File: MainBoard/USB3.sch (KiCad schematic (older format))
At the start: 16 parts, among them J10 USB3_A, J11 USB3_A (FAST), J5 USB3_A, J6 USB3_A, J8 USB3_A(INTEARNAL), J9 USB3_A, U4 TUSB8041, U5 UPD720201K8-711-BAC-A, U6 MX25L5121EMC-20G, Y1 24Mhz

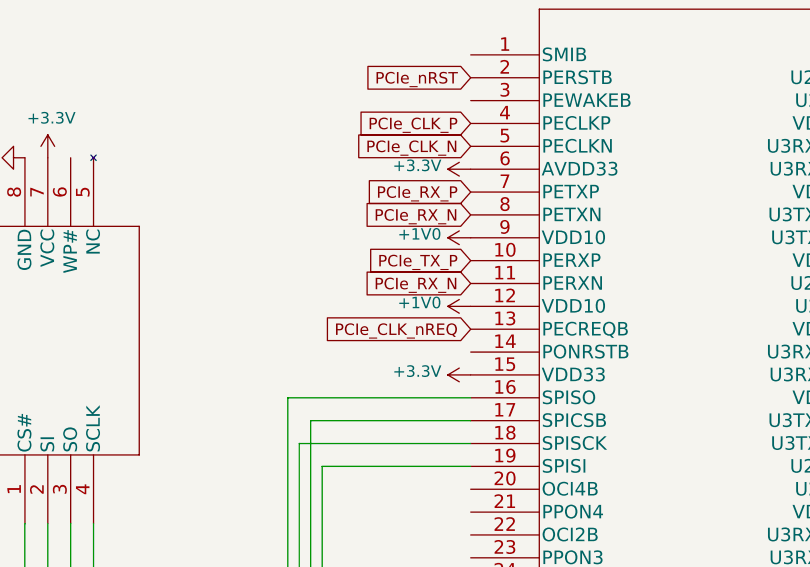
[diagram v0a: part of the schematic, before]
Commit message: finish keyboard, do some USB/PCIe routing
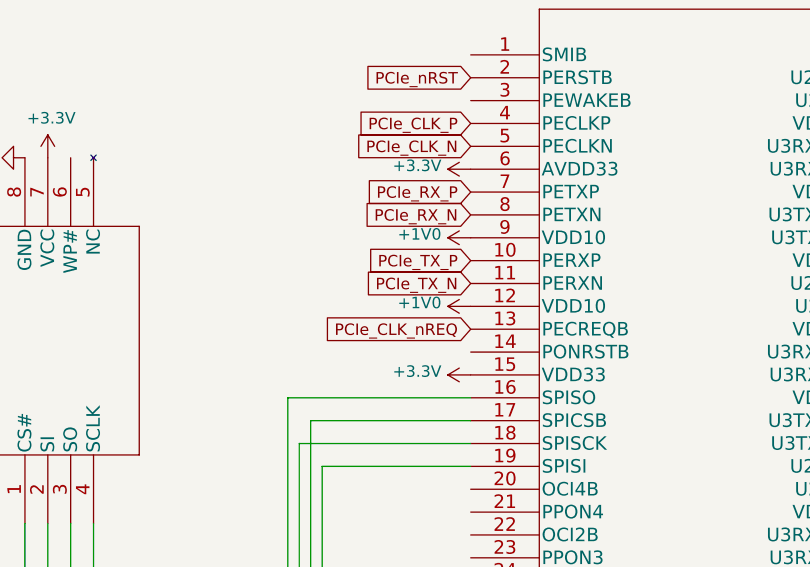
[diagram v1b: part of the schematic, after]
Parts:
- U5: footprint QFN68_8X8_REN -> Libs:UPD720201K8-711-BAC-A
- U6: footprint SOP-8L_3P9X4P9_MAC -> Libs:MX25L5121EMC-20G
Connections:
- net PCIe_RX_N: no longer U5.11 (PERXN)
- new net PCIe_TX_N: U5.11 (PERXN)
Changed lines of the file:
@@
 F 0 "U5" H 3950 4787 60  0000 C CNN
 F 1 "UPD720201K8-711-BAC-A" H 3950 4681 60  0000 C CNN
-F 2 "QFN68_8X8_REN" H 3950 4640 60  0001 C CNN
+F 2 "Libs:UPD720201K8-711-BAC-A" H 3950 4640 60  0001 C CNN
 F 3 "" H 2950 4400 60  0000 C CNN
 	1    2950 4400
@@
 PCIe_TX_P
 Text GLabel 2950 5400 0    50   Input ~ 0
-PCIe_RX_N
+PCIe_TX_N
 Text GLabel 2950 5600 0    50   Input ~ 0
 PCIe_CLK_nREQ
@@
 F 0 "U6" H 1800 6837 60  0000 C CNN
 F 1 "MX25L5121EMC-20G" H 1800 6731 60  0000 C CNN
-F 2 "SOP-8L_3P9X4P9_MAC" H 1800 6690 60  0001 C CNN
+F 2 "Libs:MX25L5121EMC-20G" H 1800 6690 60  0001 C CNN
 F 3 "" H 1000 6450 60  0000 C CNN
 	1    1000 6450

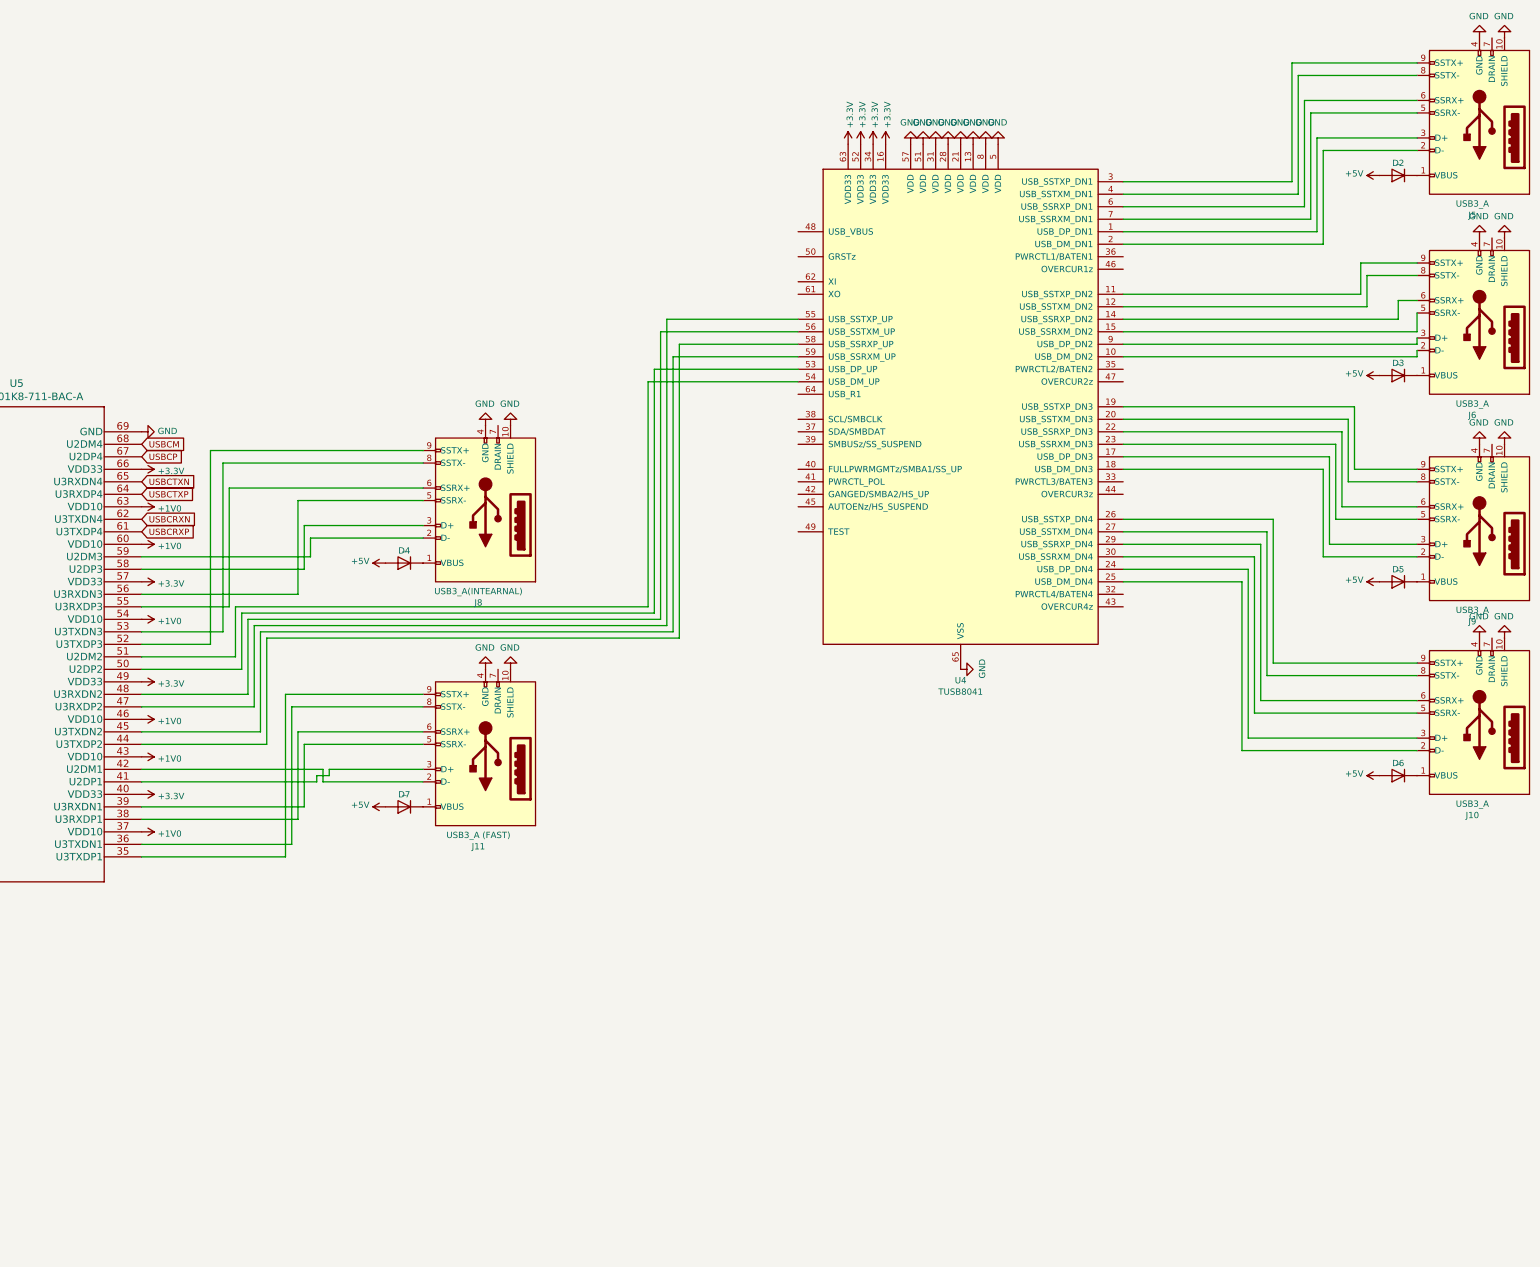
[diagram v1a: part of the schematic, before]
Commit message: remove USB ss HUB IC and add onboard USB SATA bridge
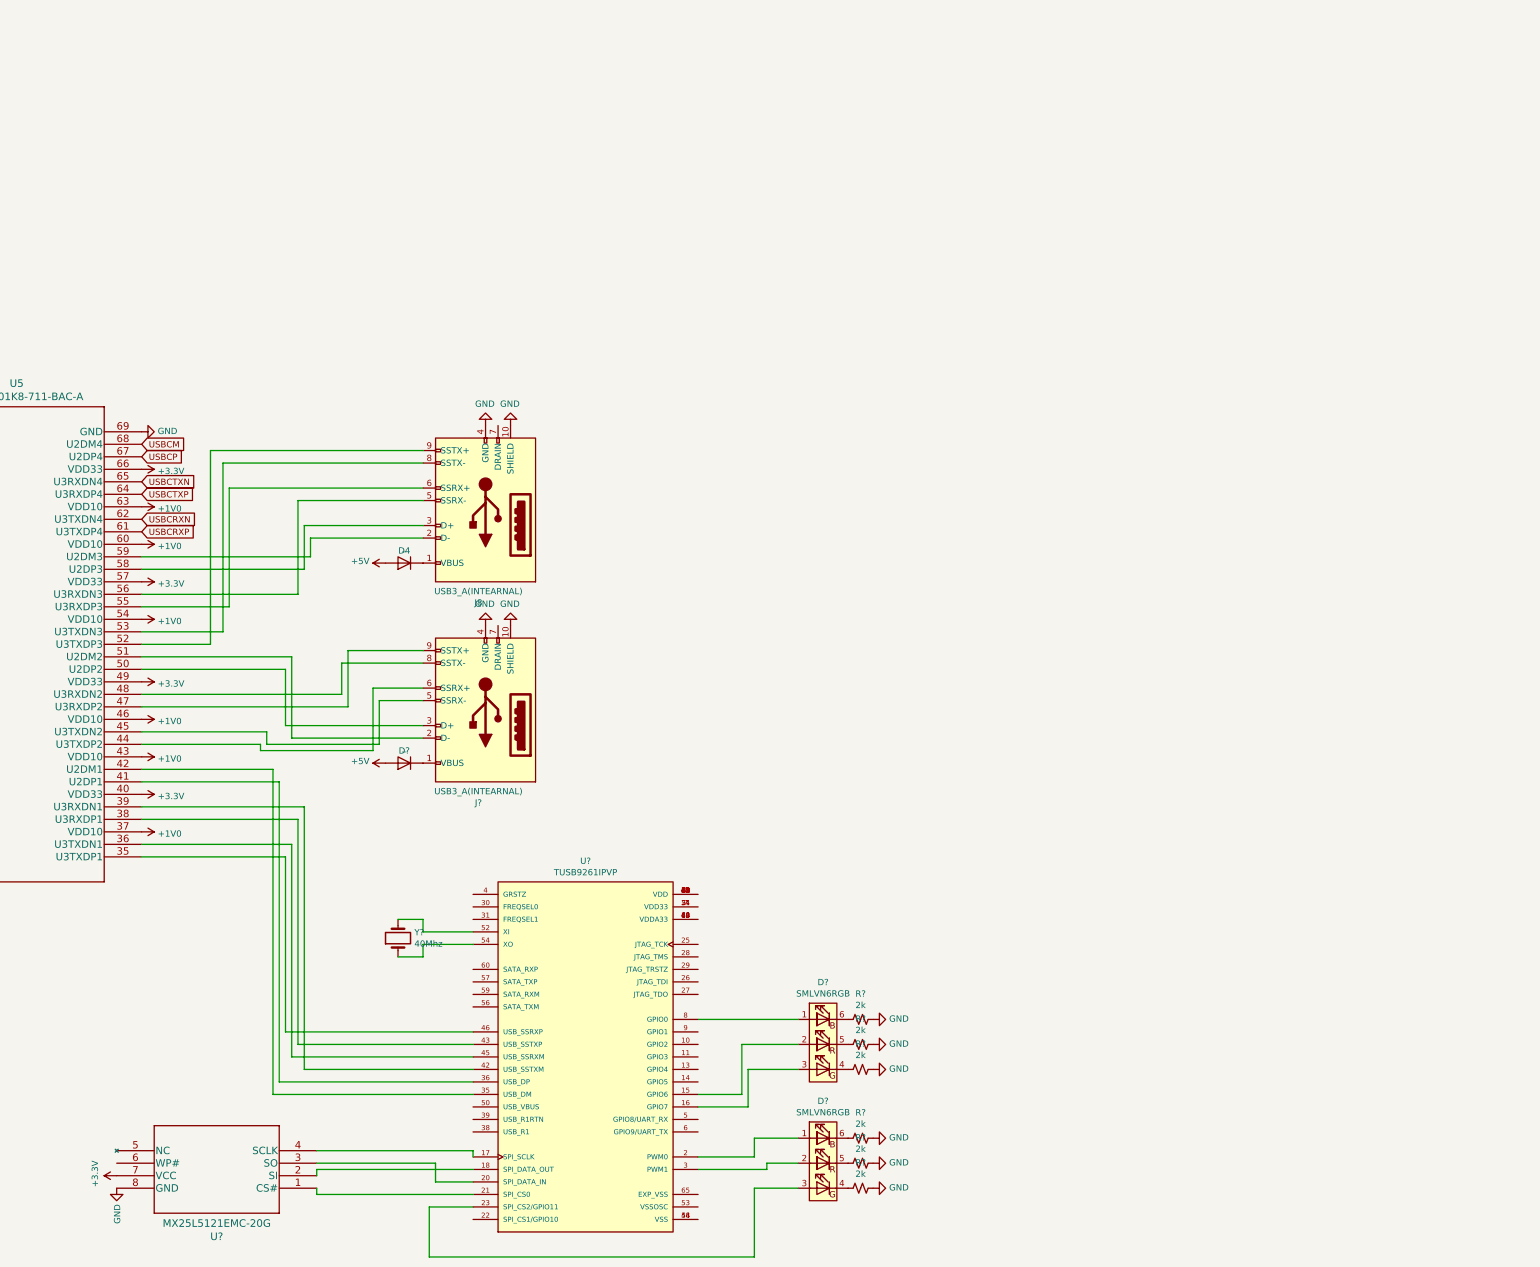
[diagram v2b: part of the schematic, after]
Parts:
- removed D2, D3, D5, D6, D7: _, symbol Simulation_SPICE:DIODE
- removed J10, J5, J6, J9: USB3_A, Connector_USB:USB3_A_Plug_Wuerth_692112030100_Horizontal, symbol Connector:USB3_A
- removed J11: USB3_A (FAST), Connector_USB:USB3_A_Plug_Wuerth_692112030100_Horizontal, symbol Connector:USB3_A
- removed U4: TUSB8041, Package_DFN_QFN:QFN-64-1EP_9x9mm_P0.5mm_EP6x6mm_ThermalVias, symbol Interface_USB:TUSB8041
- added D?: _, symbol Simulation_SPICE:DIODE
- added D? (x2): SMLVN6RGB, LED_SMD:LED_ROHM_SMLVN6, symbol LED:SMLVN6RGB
- added J?: USB3_A(INTEARNAL), symbol Connector:USB3_A
- added R? (x6): 2k, symbol Device:R_Small_US
- added U?: TUSB9261IPVP, QFP40P900X900X120-65N, symbol TUSB9261IPVP:TUSB9261IPVP
- added U?: MX25L5121EMC-20G, Libs:MX25L5121EMC-20G, symbol MX25L5121EMC:MX25L5121EMC-20G
- added Y?: 40Mhz, symbol Device:Crystal
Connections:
- net +3V3: now also U?.7 (VCC)
- net +5V: now also D?.1 (A)
- net GND: now also J?.10 (SHIELD), J?.4 (GND), R?.1, R?.1, R?.1, R?.1, R?.1, R?.1, U?.8 (GND)
- net at U5.35 (U3TXDP1): now also U?.46 (USB_SSRXP)
- net at U5.36 (U3TXDN1): now also U?.45 (USB_SSRXM)
- net at U5.38 (U3RXDP1): now also U?.43 (USB_SSTXP)
- net at U5.39 (U3RXDN1): now also U?.42 (USB_SSTXM)
- net at U5.41 (U2DP1): now also U?.36 (USB_DP)
- net at U5.42 (U2DM1): now also U?.35 (USB_DM)
- net at U5.44 (U3TXDP2): now also J?.6 (SSRX+)
- net at U5.45 (U3TXDN2): now also J?.5 (SSRX-)
- net at U5.47 (U3RXDP2): now also J?.9 (SSTX+)
- net at U5.48 (U3RXDN2): now also J?.8 (SSTX-)
- net at U5.50 (U2DP2): now also J?.3 (D+)
- net at U5.51 (U2DM2): now also J?.2 (D-)
- new net: D?.2 (K), J?.1 (VBUS)
- new net: U?.1 (VDD), U?.12 (VDD), U?.19 (VDD), U?.32 (VDD), U?.33 (VDD), U?.41 (VDD), U?.47 (VDD), U?.49 (VDD), U?.55 (VDD), U?.61 (VDD), U?.63 (VDD)
- new net: D?.2 (RA), U?.15 (GPIO6)
- new net: D?.3 (GA), U?.16 (GPIO7)
- new net: U?.17 (SPI_SCLK), U?.4 (SCLK)
- new net: U?.18 (SPI_DATA_OUT), U?.2 (SI)
- new net: D?.1 (BA), U?.2 (PWM0)
- new net: U?.20 (SPI_DATA_IN), U?.3 (SO)
- new net: U?.1 (CS#), U?.21 (SPI_CS0)
- new net: D?.3 (GA), U?.23 (SPI_CS2/GPIO11)
- new net: U?.24 (VDD33), U?.51 (VDD33), U?.7 (VDD33)
- new net: D?.2 (RA), U?.3 (PWM1)
- new net: U?.34 (VDDA33), U?.40 (VDDA33), U?.48 (VDDA33), U?.62 (VDDA33)
- new net: U?.44 (VSS), U?.58 (VSS)
- new net: U?.52 (XI), Y?.2
- new net: U?.54 (XO), Y?.1
- new net: D?.1 (BA), U?.8 (GPIO0)
- new net: D?.4 (GK), R?.2 (x2)
- new net: D?.5 (RK), R?.2 (x2)
- new net: D?.6 (BK), R?.2 (x2)
